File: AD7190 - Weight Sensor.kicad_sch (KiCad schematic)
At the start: 42 parts, among them Q1 SI2303CDS-T1-GE3, U1 AD7190WBRUZ, Y2 CSTCR4M91G53-R0

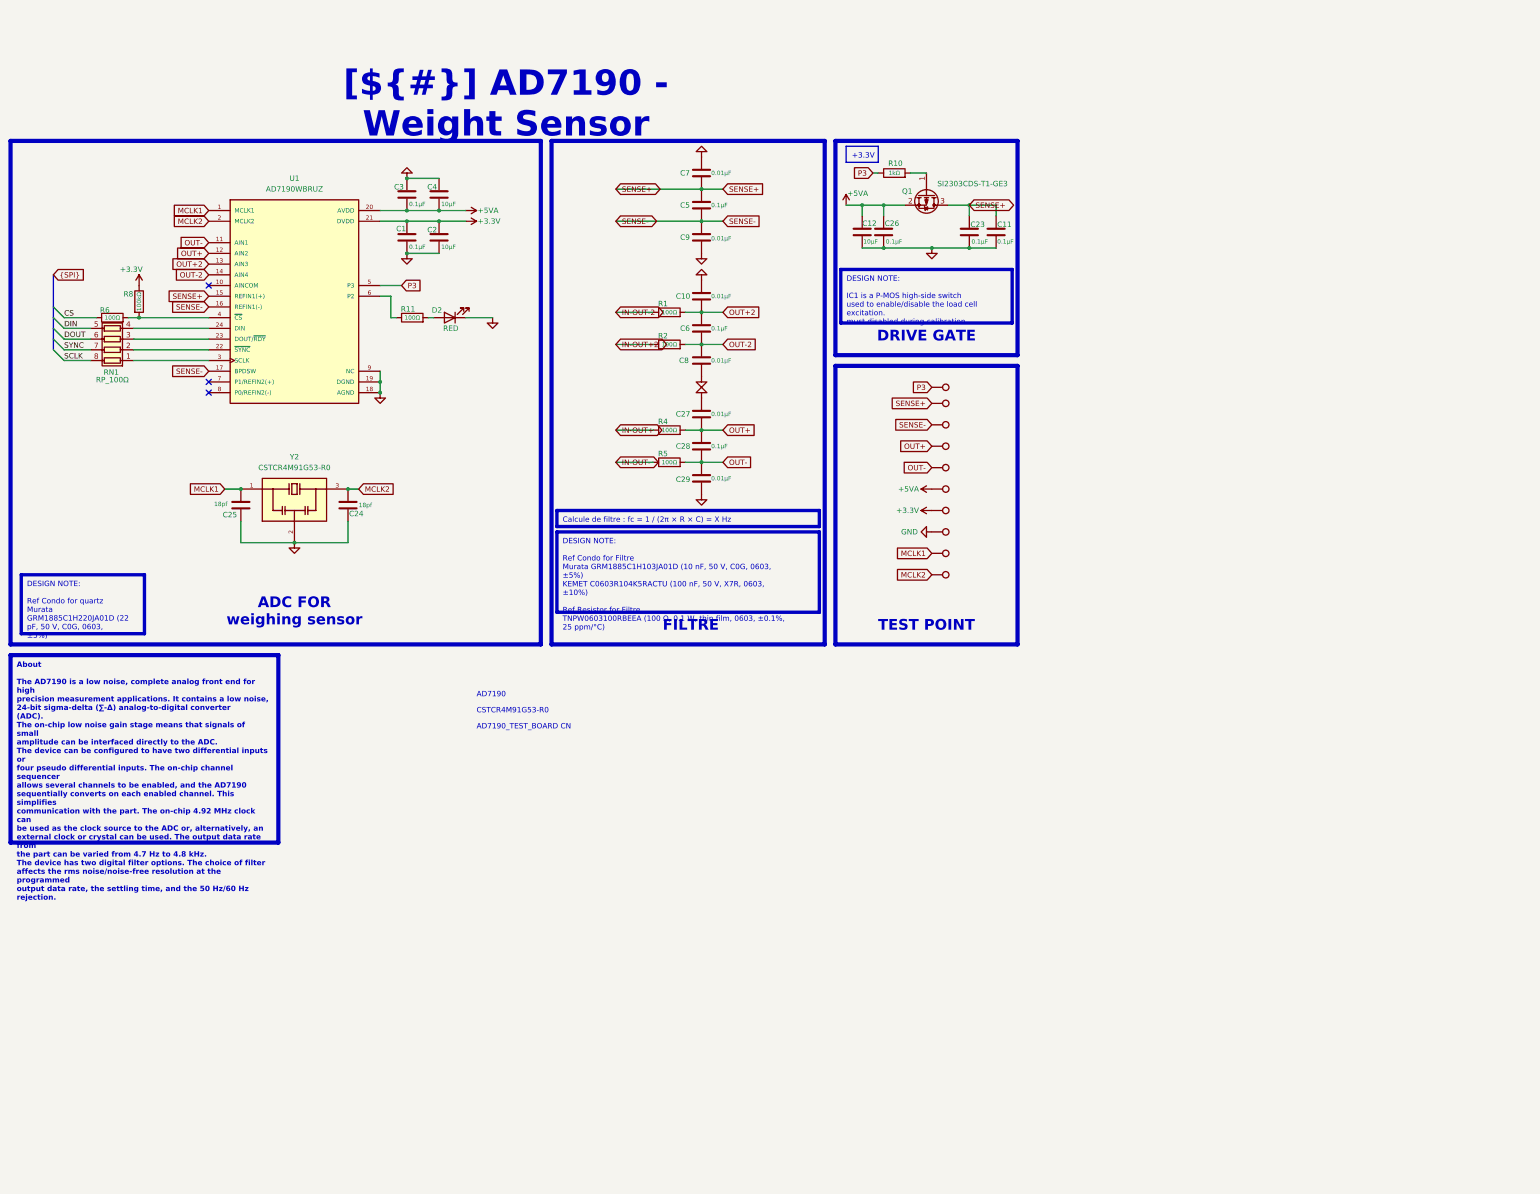
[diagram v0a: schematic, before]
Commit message: Restyle the schematic like OPEN_PHASE, merge the power sheets, rework the bottom silkscreen
- Schematic: all sheets on A3 in the OPEN_PHASE look (red header bands,
  DESCRIPTION / DESIGN NOTE / LAYOUT NOTE / CALCULS & BUDGET panels in
  French, TEST POINTS panel, References in the title block)
- Title block: INGENIERIE FRANCE logo in KDT_Template_GIT.kicad_wks,
  per-sheet logo images removed
- Power - Sequencing rebuilt with curves from LTspice simulations 01-04
- TPS61086 and LT3042 sheets merged into Power Supply - Analog Rails
  (page 5, keeps the TPS sheet UUID); pages renumbered to 9, local nets
  renamed to /Project Architecture/Power_Supply/*, PCB links updated
- PCB: per-rail net colours (+3.3V, +6V, +5VA, GND) as on OPEN_PHASE
- PCB B.SilkS: test point pills with Arial Black knockout names, J1
  pinout cells, E+/E-/S+/S- tags on the M12 pads, CELL 1 / CELL 2 titles
  and a LOAD CELL wiring panel

Netlist connectivity, ERC (2 warnings) and copper DRC unchanged;
schematic parity clean.

Co-Authored-By: Claude Opus 5.5 <noreply@anthropic.com>
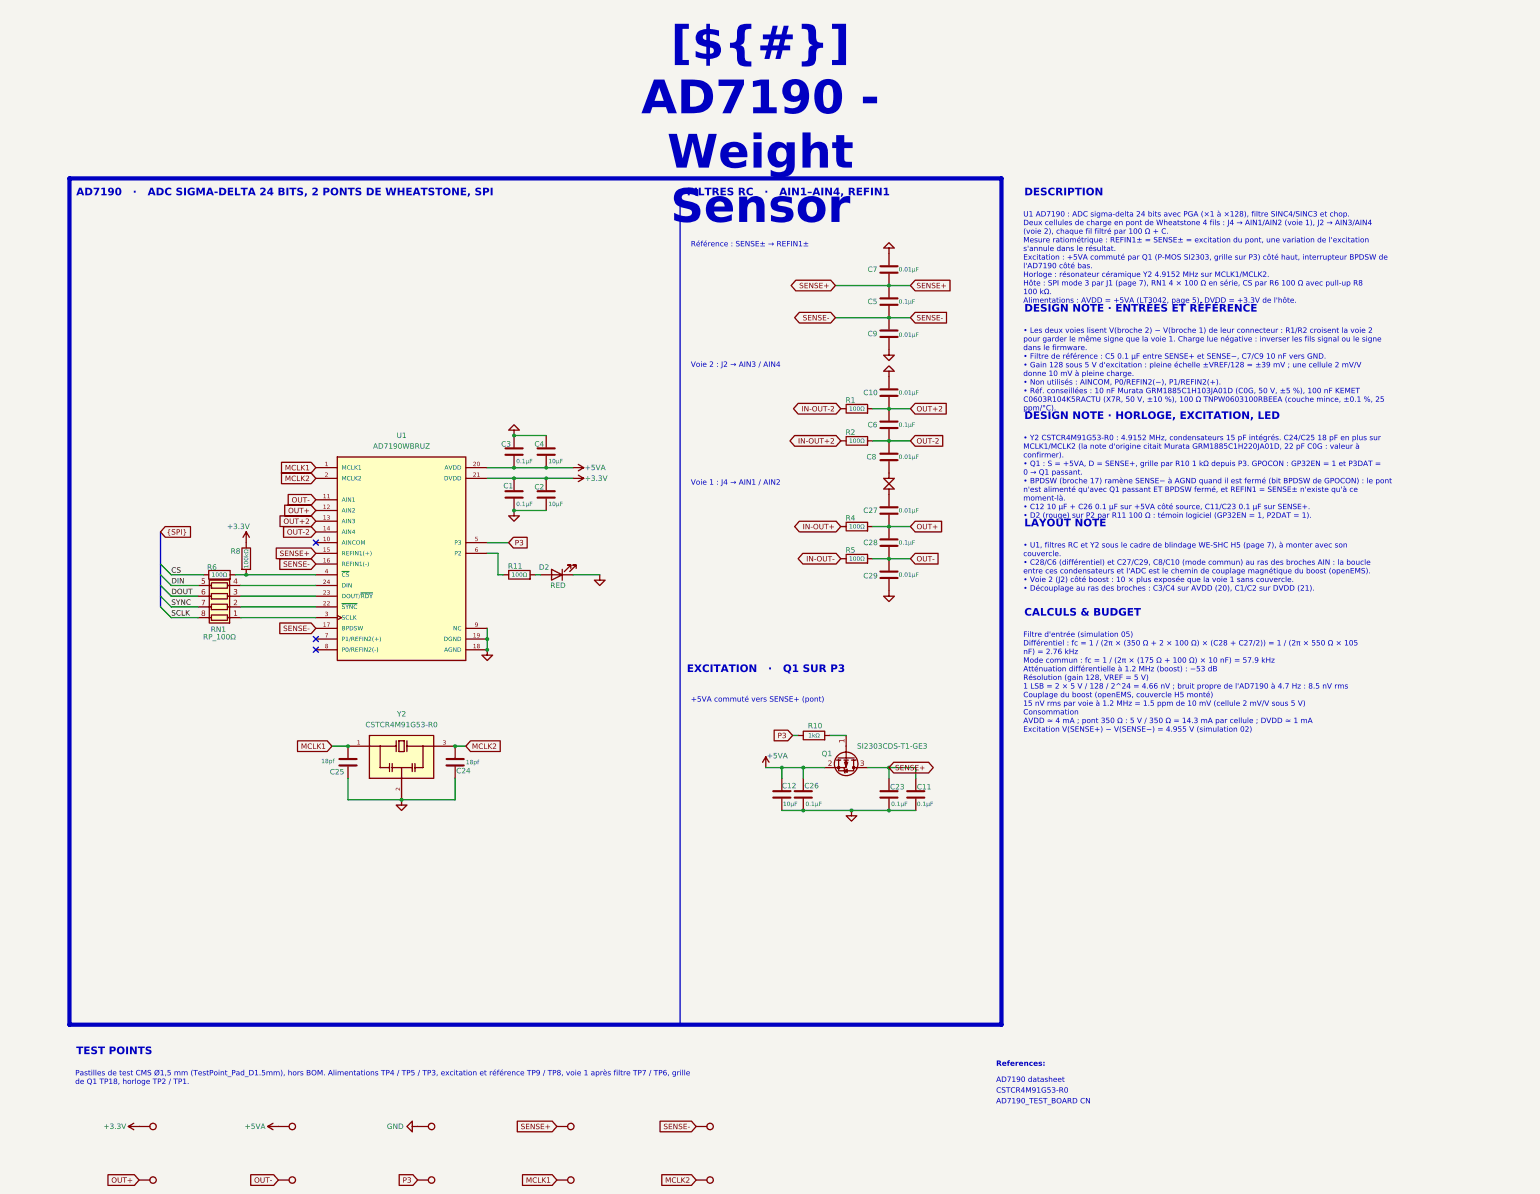
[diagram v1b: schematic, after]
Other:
- note added: "+5VA commuté vers SENSE+ (pont)"
- note added: "AD7190 datasheet"
- note added: "References:"
- note added: "Référence : SENSE± → REFIN1±"
- note added: "Voie 1 : J4 → AIN1 / AIN2"
- note added: "Voie 2 : J2 → AIN3 / AIN4"
- note removed: "AD7190"
- moved on the sheet: C1, C10, C11, C12, C2, C23, C24, C25, C26, C27, C28, C29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
